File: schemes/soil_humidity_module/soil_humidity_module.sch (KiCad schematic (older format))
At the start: 9 parts, among them Q1 IRL540N, Q2 BC547, U1 nRF24L01P, U2 SEN0193

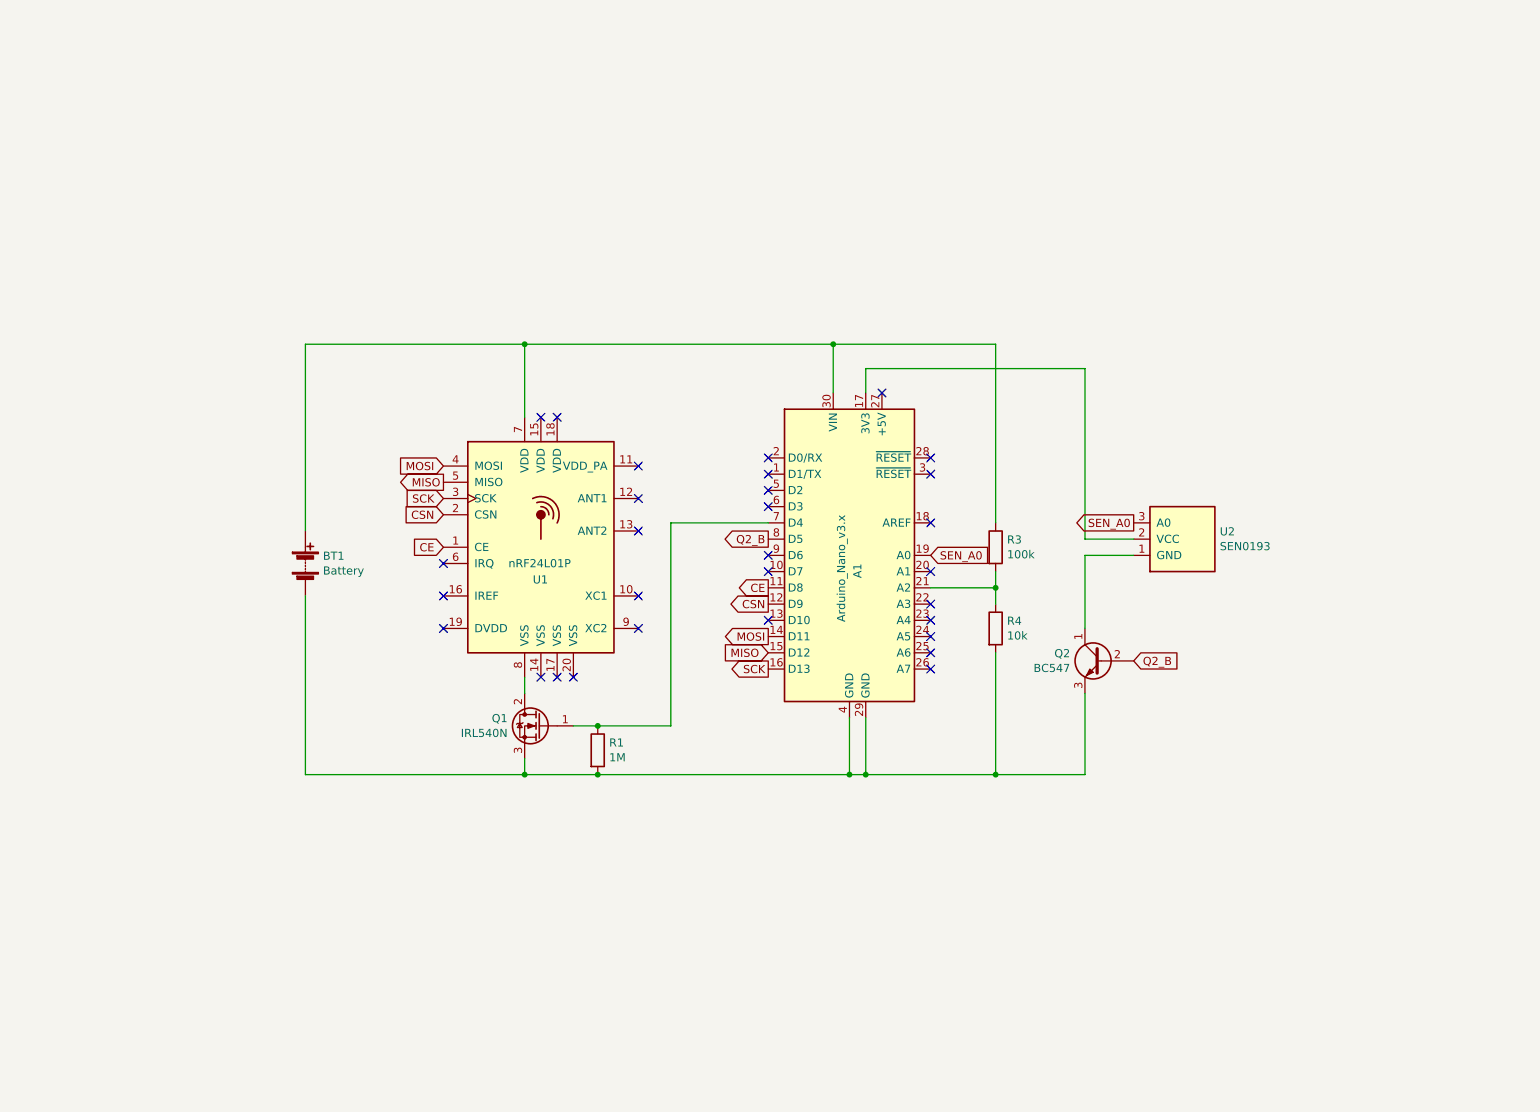
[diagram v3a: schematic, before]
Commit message: [soil_humidity_transmitter] Simplification of the circuit
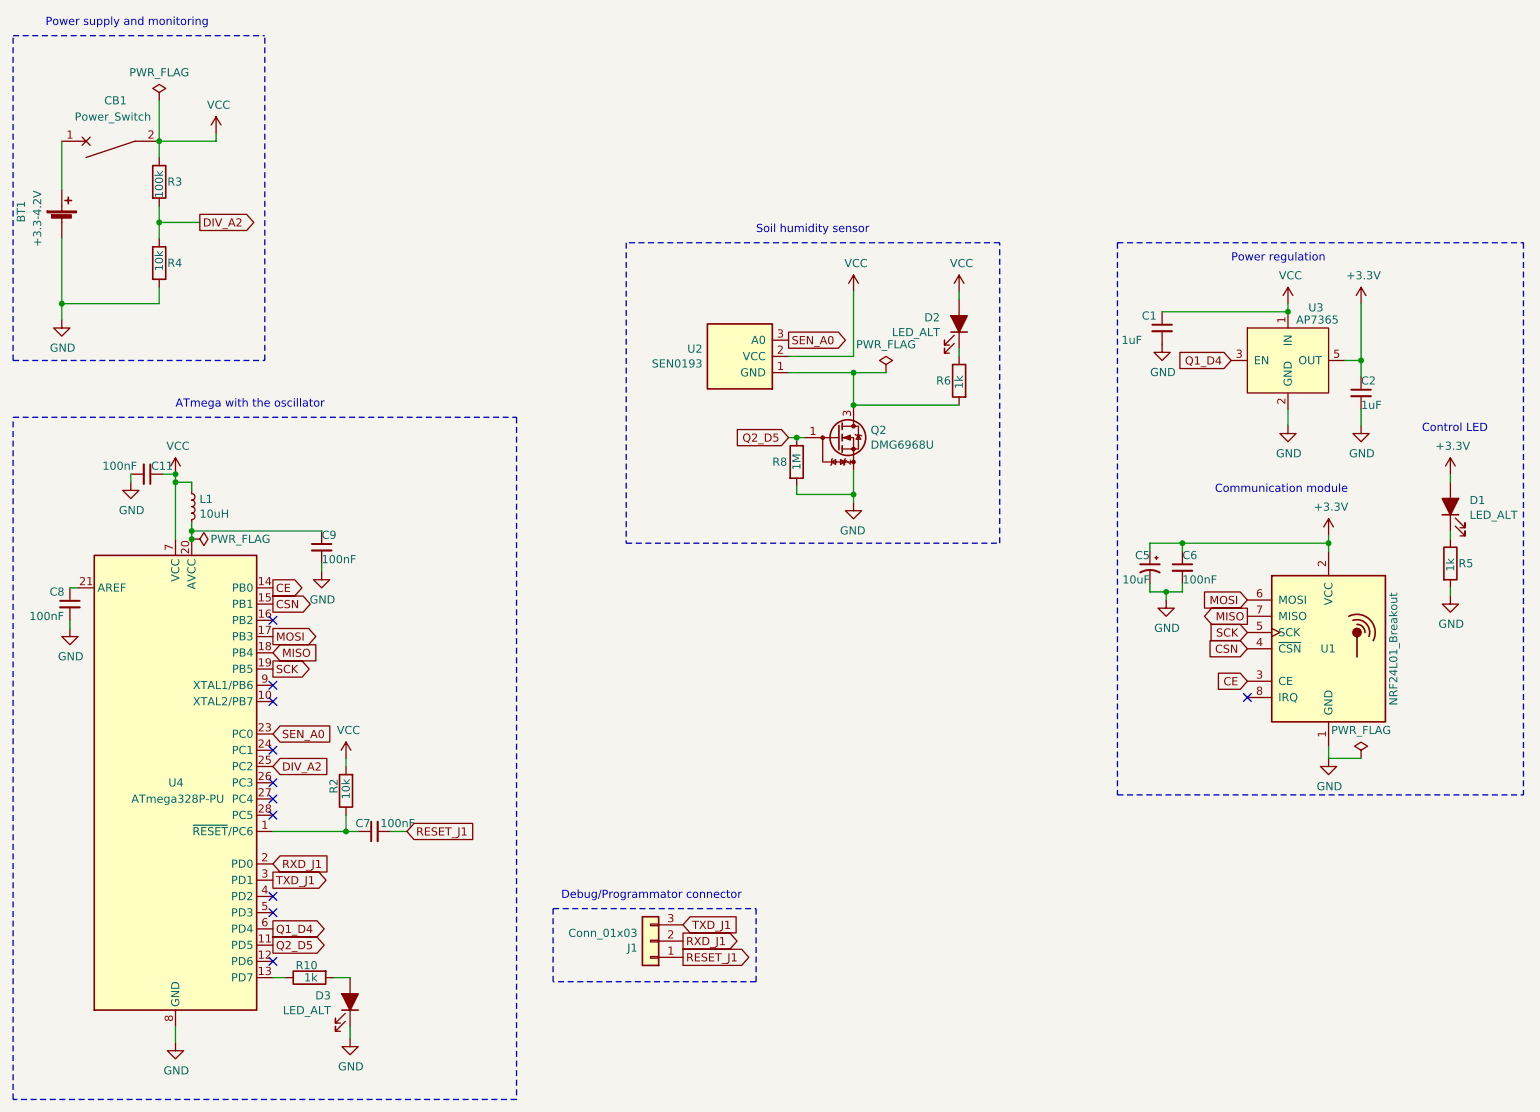
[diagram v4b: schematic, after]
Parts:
- removed A1: Arduino_Nano_v3.x, Module:Arduino_Nano, symbol MCU_Module:Arduino_Nano_v3.x
- removed BT1: Battery, Connector_AMASS:AMASS_XT30U-F_1x02_P5.0mm_Vertical, symbol Device:Battery
- removed Q1: IRL540N, Package_TO_SOT_THT:TO-220-3_Vertical, symbol soil_humidity_module:IRL540N
- removed Q2: BC547, Package_TO_SOT_THT:TO-92_Inline, symbol Transistor_BJT:BC547
- removed R1: 1M, Resistor_SMD:R_0805_2012Metric_Pad1.15x1.40mm_HandSolder, symbol Device:R
- removed U1: nRF24L01P, Connector_PinHeader_2.54mm:PinHeader_2x04_P2.54mm_Vertical, symbol RF:nRF24L01P
- added BT1: +3.3-4.2V, Connector_AMASS:AMASS_XT30U-F_1x02_P5.0mm_Vertical, symbol Device:Battery_Cell
- added C1, C2: 1uF, Capacitor_SMD:C_0805_2012Metric, symbol Device:C_Small
- added C11, C6, C7, C8, C9: 100nF, Capacitor_SMD:C_0805_2012Metric, symbol Device:C_Small
- added C5: 10uF, Capacitor_SMD:C_0805_2012Metric, symbol Device:CP1_Small
- added CB1: Power_Switch, Connector_JST:JST_XH_B2B-XH-AM_1x02_P2.50mm_Vertical, symbol Device:CircuitBreaker_1P
- added D1, D2, D3: LED_ALT, LED_SMD:LED_0805_2012Metric, symbol Device:LED_ALT
- added J1: Conn_01x03, Connector_PinHeader_2.54mm:PinHeader_1x03_P2.54mm_Vertical, symbol Connector_Generic:Conn_01x03
- added L1: 10uH, Inductor_SMD:L_0805_2012Metric, symbol Device:L_Small
- added Q2: DMG6968U, Package_TO_SOT_SMD:SOT-23, symbol soil_humidity_module:DMG6968U
- added R10, R5, R6: 1k, Resistor_SMD:R_0805_2012Metric, symbol Device:R
- added R2: 10k, Resistor_SMD:R_0805_2012Metric, symbol Device:R
- added R8: 1M, Resistor_SMD:R_0805_2012Metric, symbol Device:R
- added U1: NRF24L01_Breakout, RF_Module:nRF24L01_Breakout, symbol RF:NRF24L01_Breakout
- added U3: AP7365, Package_TO_SOT_SMD:SOT-23-5_HandSoldering, symbol soil_humidity_module:AP7365
- added U4: ATmega328P-PU, Package_DIP:DIP-28_W7.62mm, symbol MCU_Microchip_ATmega:ATmega328P-PU
- R3, R4: footprint Resistor_SMD:R_0805_2012Metric_Pad1.15x1.40mm_HandSolder -> Resistor_SMD:R_0805_2012Metric
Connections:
- net CE: now also U1.3 (CE), U4.14 (PB0)
- net CSN: now also U1.4 (~CSN), U4.15 (PB1)
- net MISO: now also U1.7 (MISO), U4.18 (PB4)
- net MOSI: now also U1.6 (MOSI), U4.17 (PB3)
- net SCK: now also U1.5 (SCK), U4.19 (PB5)
- net SEN_A0: now also U4.23 (PC0)
- net VCC: now reaches U2.2 (VCC)
- net VCC: now also R3.1, C1.1, C11.1, CB1.2, D2.2 (A), L1.1, R2.2, U3.1 (IN), U4.7 (VCC)
- net DIV_A2: now reaches R3.2, R4.1
- net DIV_A2: now also U4.25 (PC2)
- net GND: now reaches R4.2
- net GND: now also BT1.2 (-), C1.2, C11.2, C2.2, C5.2, C6.2, C8.2, C9.2, D3.1 (K), Q2.2 (S), R5.2, R8.2, U1.1 (GND), U3.2 (GND), U4.22 (GND), U4.8 (GND)
- net at U2.1 (GND): now also Q2.3 (D), R6.2
- new net: C7.1, R2.1, U4.1 (~RESET~/PC6)
- new net: R10.1, U4.13 (PD7)
- new net: C9.1, L1.2, U4.20 (AVCC)
- new net: C8.1, U4.21 (AREF)
- new net: BT1.1 (+), CB1.1
- new net: D2.1 (K), R6.1
- new net: D1.1 (K), R5.1
- new net: D3.2 (A), R10.2
- new net +3V3: C2.1, C5.1, C6.1, D1.2 (A), U1.2 (VCC), U3.5 (OUT)
- new net Q1_D4: U3.3 (EN), U4.6 (PD4)
- new net Q2_D5: Q2.1 (G), R8.1, U4.11 (PD5)
- new net RESET_J1: C7.2, J1.1 (Pin_1)
- new net RXD_J1: J1.2 (Pin_2), U4.2 (PD0)
- new net TXD_J1: J1.3 (Pin_3), U4.3 (PD1)
- no-connect marks 30 -> 11
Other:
- note added: "ATmega with the oscillator"
- note added: "Communication module"
- note added: "Control LED"
- note added: "Debug/Programmator connector"
- note added: "Power regulation"
- note added: "Power supply and monitoring"
- note added: "Soil humidity sensor"
- moved on the sheet: R3, R4, U2
